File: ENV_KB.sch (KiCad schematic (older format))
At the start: 183 parts, among them J1 TYPE-C-31-M-12

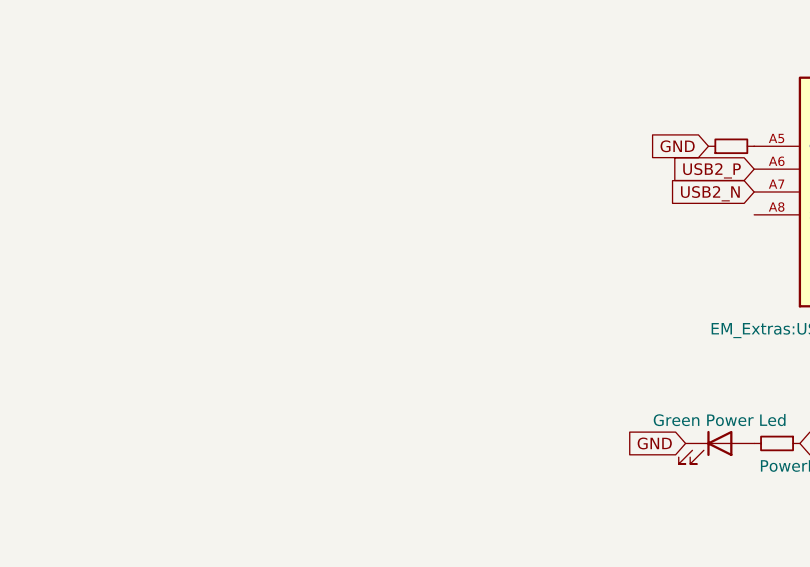
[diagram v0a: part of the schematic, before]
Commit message: Added some M2 mount holes
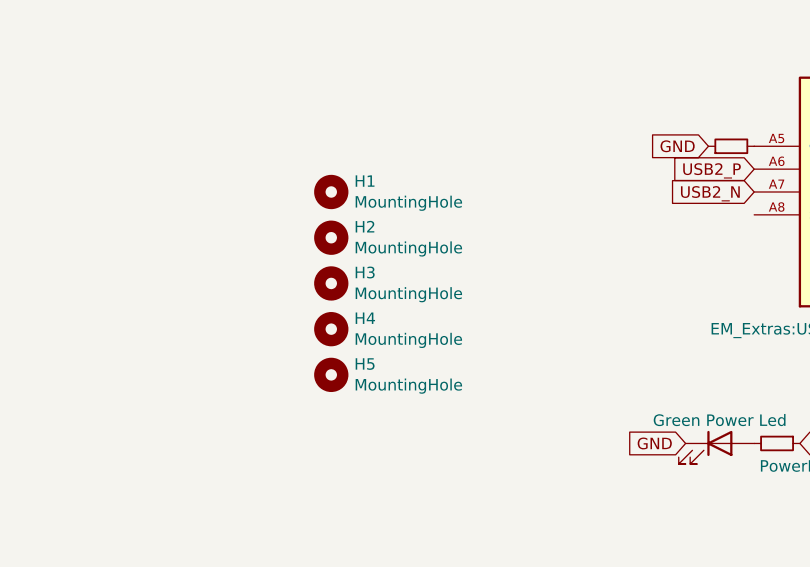
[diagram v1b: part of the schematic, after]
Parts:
- added H1, H2, H3, H4, H5: MountingHole, MountingHole:MountingHole_2.2mm_M2, symbol Mechanical:MountingHole
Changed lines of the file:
@@
 Text GLabel 13750 8250 2    50   Input ~ 0
 3.3V
+$Comp
+L Mechanical:MountingHole H4
+U 1 1 6058BC08
+P 6600 9450
+F 0 "H4" H 6700 9496 50  0000 L CNN
+F 1 "MountingHole" H 6700 9405 50  0000 L CNN
+F 2 "MountingHole:MountingHole_2.2mm_M2" H 6600 9450 50  0001 C CNN
+F 3 "~" H 6600 9450 50  0001 C CNN
+	1    6600 9450
+	1    0    0    -1
+$EndComp
+$Comp
+L Mechanical:MountingHole H3
+U 1 1 60591F15
+P 6600 9250
+F 0 "H3" H 6700 9296 50  0000 L CNN
+F 1 "MountingHole" H 6700 9205 50  0000 L CNN
+F 2 "MountingHole:MountingHole_2.2mm_M2" H 6600 9250 50  0001 C CNN
+F 3 "~" H 6600 9250 50  0001 C CNN
+	1    6600 9250
+	1    0    0    -1
+$EndComp
+$Comp
+L Mechanical:MountingHole H1
+U 1 1 605938C3
+P 6600 8850
+F 0 "H1" H 6700 8896 50  0000 L CNN
+F 1 "MountingHole" H 6700 8805 50  0000 L CNN
+F 2 "MountingHole:MountingHole_2.2mm_M2" H 6600 8850 50  0001 C CNN
+F 3 "~" H 6600 8850 50  0001 C CNN
+	1    6600 8850
+	1    0    0    -1
+$EndComp
+$Comp
+L Mechanical:MountingHole H2
+U 1 1 605BD366
+P 6600 9050
+F 0 "H2" H 6700 9096 50  0000 L CNN
+F 1 "MountingHole" H 6700 9005 50  0000 L CNN
+F 2 "MountingHole:MountingHole_2.2mm_M2" H 6600 9050 50  0001 C CNN
+F 3 "~" H 6600 9050 50  0001 C CNN
+	1    6600 9050
+	1    0    0    -1
+$EndComp
+$Comp
+L Mechanical:MountingHole H5
+U 1 1 6068A680
+P 6600 9650
+F 0 "H5" H 6700 9696 50  0000 L CNN
+F 1 "MountingHole" H 6700 9605 50  0000 L CNN
+F 2 "MountingHole:MountingHole_2.2mm_M2" H 6600 9650 50  0001 C CNN
+F 3 "~" H 6600 9650 50  0001 C CNN
+	1    6600 9650
+	1    0    0    -1
+$EndComp
 $EndSCHEMATC

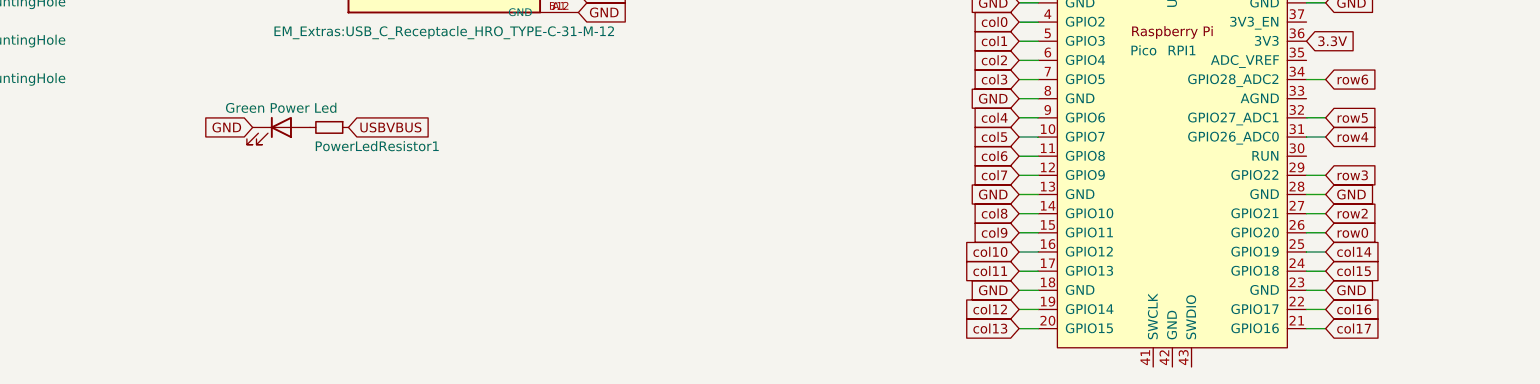
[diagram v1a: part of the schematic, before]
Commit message: Added Reset Button, Adjusted some trace routes, Updated Schematic
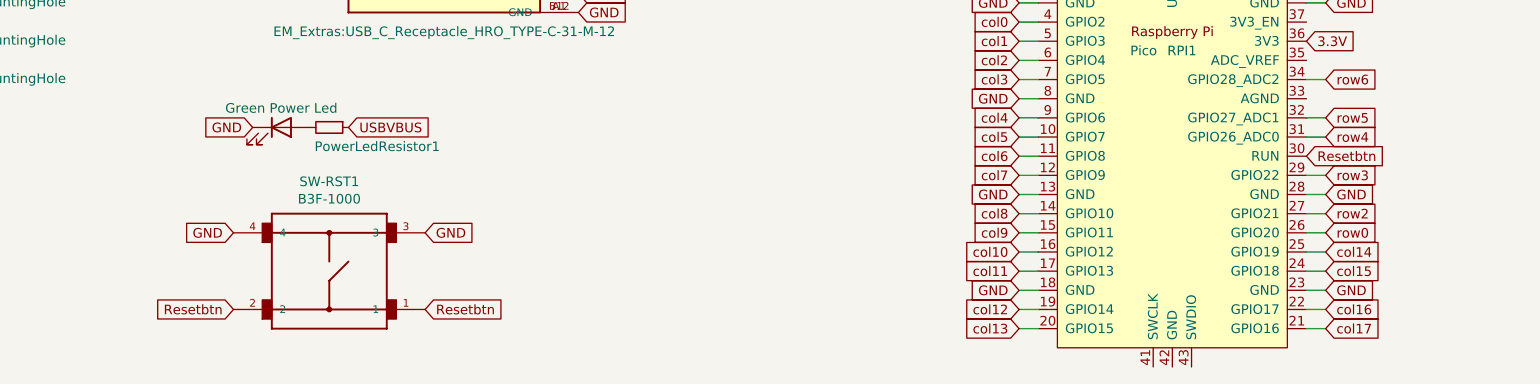
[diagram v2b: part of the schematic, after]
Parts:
- added SW-RST1: B3F-1000, EM_Extras:SW_B3F-1000, symbol B3F-1000:B3F-1000
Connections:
- net GND: now also SW-RST1.3, SW-RST1.4
- net Resetbtn: now reaches RPI1.30 (RUN)
- net Resetbtn: now also SW-RST1.1, SW-RST1.2
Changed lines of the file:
@@
 	1    0    0    -1
 $EndComp
+Text GLabel 13650 10100 2    50   Input ~ 0
+Resetbtn
+Text GLabel 9050 10500 2    50   Input ~ 0
+GND
+Text GLabel 8050 10900 0    50   Input ~ 0
+Resetbtn
+$Comp
+L B3F-1000:B3F-1000 SW-RST1
+U 1 1 605FBFA6
+P 8550 10700
+F 0 "SW-RST1" H 8550 11167 50  0000 C CNN
+F 1 "B3F-1000" H 8550 11076 50  0000 C CNN
+F 2 "EM_Extras:SW_B3F-1000" H 8550 10700 50  0001 L BNN
+F 3 "" H 8550 10700 50  0001 L BNN
+F 4 "Omron" H 8550 10700 50  0001 L BNN "MANUFACTURER"
+	1    8550 10700
+	1    0    0    -1
+$EndComp
+Text GLabel 8050 10500 0    50   Input ~ 0
+GND
+Text GLabel 9050 10900 2    50   Input ~ 0
+Resetbtn
 $EndSCHEMATC

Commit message: Initial Ansi Support
adding support to fit ansi backslash and enter key

probably needs some double checking +this would be incompatible with the current keymap unless you dont mind a non functional enter key and a ANSI backslash which does enter instead.
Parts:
- added D63: D, CFTKB Bits:D_DO-35_SOD27_P5.08mm_Horizontal, symbol Device:D_Small
- added K_63: MX-NoLED, MX_only:MXOnly-ISO-ROTATED-ReversedStabilizers-NoLED, symbol MX_Alps_Hybrid:MX-NoLED
- added K_63B1: MX-NoLED, MX_only:MXOnly-2.25U-NoLED, symbol MX_Alps_Hybrid:MX-NoLED
- added K_64B1: KEYSW, MX_only:MXOnly-2.25U-NoLED, symbol MX_Alps_Hybrid:MX-NoLED
- K_46: footprint MX_only:MXOnly-ISO-ROTATED-ReversedStabilizers-NoLED -> MX_only:MXOnly-1.5U-NoLED
- renumbered D63 to D64, D64 to D65, D65 to D66, D66 to D67, D67 to D68, D68 to D69, D69 to D70, D70 to D71, D71 to D72, D72 to D73, D73 to D74, D74 to D75, D75 to D76, D76 to D77, D77 to D78, D78 to D79, D79 to D80, D80 to D81, D81 to D82, D82 to D83, D83 to D84, D84 to D85, D85 to D86, D86 to D87, D87 to D88, H1 to H0, H2 to H1, H3 to H2, H4 to H3, H5 to H4, I2CHeader1 to I2CHeader0, J1 to J0, K_63 to K_64, K_64 to K_65, K_65 to K_66, K_66 to K_67, K_67 to K_68, K_68 to K_69, K_69 to K_70, K_70 to K_71, K_71 to K_72, K_72 to K_73, K_73 to K_74, K_74 to K_75, K_75 to K_76, K_76 to K_77, K_77 to K_78, K_78 to K_79, K_79 to K_80, K_80 to K_81, K_81 to K_82, K_82 to K_83, K_83 to K_84, K_84 to K_85, K_85 to K_86, K_86 to K_87, K_87 to K_88, PowerLED1 to PowerLED0, PowerLedResistor1 to PowerLedResistor0, RESISTOR2 to RESISTOR0, RPI1 to RPI0, SW-RST1 to SW-RST0
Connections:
- net col0: now also K_64B1.1 (COL)
- net col14: now also K_63.1 (COL), K_63B1.1 (COL)
- net row4: now also D63.1 (K)
- net at D64.2 (A), K_64.2 (ROW): now also K_64B1.2 (ROW)
- new net: D63.2 (A), K_63.2 (ROW), K_63B1.2 (ROW)

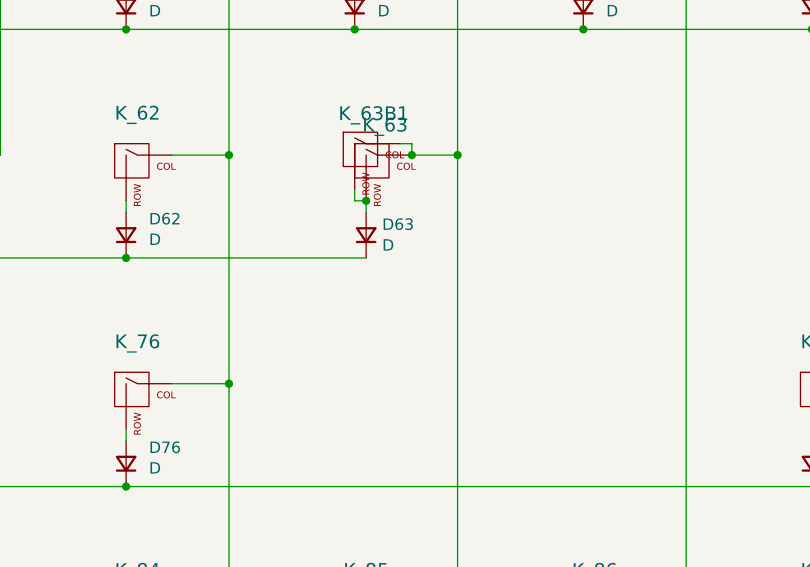
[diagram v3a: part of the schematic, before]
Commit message: ANSI updates and cleaning up
just neatened up some traces, added some markings.
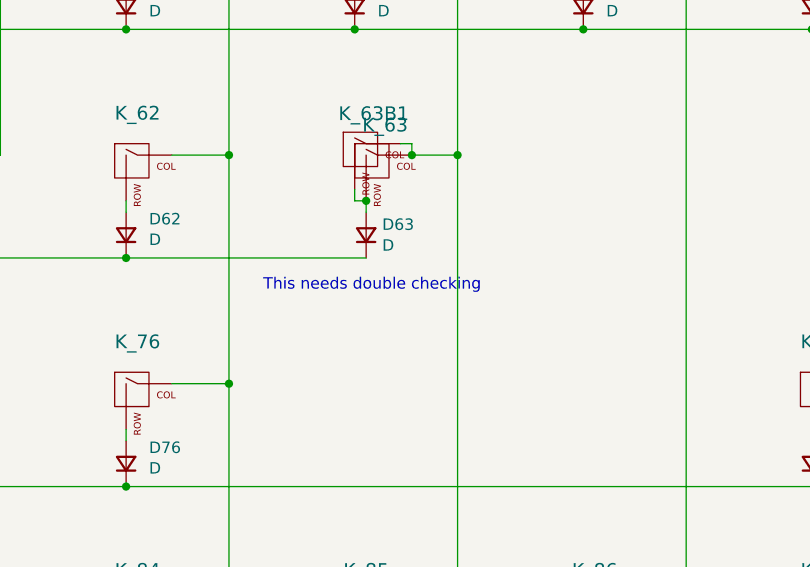
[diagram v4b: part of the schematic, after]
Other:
- note added: "This needs double checking"
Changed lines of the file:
@@
 	1550 5900 1500 5900
 Connection ~ 1550 5950
+Text Notes 14950 5550 0    50   ~ 0
+This needs double checking
 $EndSCHEMATC

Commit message: more plate design work + screwholes
I would like for this keyboard to feel like a solid unit like a individual object not an assembly of a few, something sturdy and light.
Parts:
- added H5, H6, H7, H8: MountingHole, MountingHole:MountingHole_2.2mm_M2, symbol Mechanical:MountingHole
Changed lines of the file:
@@
 Text Notes 14950 5550 0    50   ~ 0
 This needs double checking
+$Comp
+L Mechanical:MountingHole H5
+U 1 1 606F0C32
+P 6600 9850
+F 0 "H5" H 6700 9896 50  0000 L CNN
+F 1 "MountingHole" H 6700 9805 50  0000 L CNN
+F 2 "MountingHole:MountingHole_2.2mm_M2" H 6600 9850 50  0001 C CNN
+F 3 "~" H 6600 9850 50  0001 C CNN
+	1    6600 9850
+	1    0    0    -1
+$EndComp
+$Comp
+L Mechanical:MountingHole H6
+U 1 1 60748B43
+P 6600 10050
+F 0 "H6" H 6700 10096 50  0000 L CNN
+F 1 "MountingHole" H 6700 10005 50  0000 L CNN
+F 2 "MountingHole:MountingHole_2.2mm_M2" H 6600 10050 50  0001 C CNN
+F 3 "~" H 6600 10050 50  0001 C CNN
+	1    6600 10050
+	1    0    0    -1
+$EndComp
+$Comp
+L Mechanical:MountingHole H7
+U 1 1 6077360A
+P 6600 10250
+F 0 "H7" H 6700 10296 50  0000 L CNN
+F 1 "MountingHole" H 6700 10205 50  0000 L CNN
+F 2 "MountingHole:MountingHole_2.2mm_M2" H 6600 10250 50  0001 C CNN
+F 3 "~" H 6600 10250 50  0001 C CNN
+	1    6600 10250
+	1    0    0    -1
+$EndComp
+$Comp
+L Mechanical:MountingHole H8
+U 1 1 607CB78F
+P 6600 10450
+F 0 "H8" H 6700 10496 50  0000 L CNN
+F 1 "MountingHole" H 6700 10405 50  0000 L CNN
+F 2 "MountingHole:MountingHole_2.2mm_M2" H 6600 10450 50  0001 C CNN
+F 3 "~" H 6600 10450 50  0001 C CNN
+	1    6600 10450
+	1    0    0    -1
+$EndComp
 $EndSCHEMATC

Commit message: Adding more mount holes and some alignment adjustments
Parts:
- added H10, H9: MountingHole, MountingHole:MountingHole_2.2mm_M2, symbol Mechanical:MountingHole
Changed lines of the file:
@@
+	1    0    0    -1
+$EndComp
+$Comp
+L Mechanical:MountingHole H9
+U 1 1 60717F95
+P 6600 10650
+F 0 "H9" H 6700 10696 50  0000 L CNN
+F 1 "MountingHole" H 6700 10605 50  0000 L CNN
+F 2 "MountingHole:MountingHole_2.2mm_M2" H 6600 10650 50  0001 C CNN
+F 3 "~" H 6600 10650 50  0001 C CNN
+	1    6600 10650
+	1    0    0    -1
+$EndComp
+$Comp
+L Mechanical:MountingHole H10
+U 1 1 607429B3
+P 6600 10850
+F 0 "H10" H 6700 10896 50  0000 L CNN
+F 1 "MountingHole" H 6700 10805 50  0000 L CNN
+F 2 "MountingHole:MountingHole_2.2mm_M2" H 6600 10850 50  0001 C CNN
+F 3 "~" H 6600 10850 50  0001 C CNN
+	1    6600 10850
 	1    0    0    -1
 $EndComp

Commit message: Some small updates and corrections
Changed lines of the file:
@@
+	1    0    0    -1
+$EndComp
+$Comp
+L PersonalLogo:LOGO #G1
+U 1 1 607C9850
+P 5000 9700
+F 0 "#G1" H 5000 9090 60  0001 C CNN
+F 1 "LOGO" H 5000 10310 60  0001 C CNN
+F 2 "" H 5000 9700 50  0001 C CNN
+F 3 "" H 5000 9700 50  0001 C CNN
+	1    5000 9700
 	1    0    0    -1
 $EndComp

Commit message: added B§F-100o back to Symbole Lib Back pasting of my changes move of drill hole lower right side
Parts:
- removed D63: D, CFTKB Bits:D_DO-35_SOD27_P5.08mm_Horizontal, symbol Device:D_Small
- removed H10, H5, H6, H7, H8, H9: MountingHole, MountingHole:MountingHole_2.2mm_M2, symbol Mechanical:MountingHole
- removed K_63: MX-NoLED, MX_only:MXOnly-ISO-ROTATED-ReversedStabilizers-NoLED, symbol MX_Alps_Hybrid:MX-NoLED
- removed K_63B1: MX-NoLED, MX_only:MXOnly-2.25U-NoLED, symbol MX_Alps_Hybrid:MX-NoLED
- removed K_64B1: KEYSW, MX_only:MXOnly-2.25U-NoLED, symbol MX_Alps_Hybrid:MX-NoLED
- added D100, D101, D102, D103, D104, D88, D89, D90, D91, D92, D93, D94, D95, D96, D97, D98, D99: D, CFTKB Bits:D_DO-35_SOD27_P5.08mm_Horizontal, symbol Device:D_Small
- added D105: Scroll Lock, LED_THT:LED_D5.0mm, symbol Device:LED
- added D106: Cabs Lock, LED_THT:LED_D5.0mm, symbol Device:LED
- added D107: NUM Lock, LED_THT:LED_D5.0mm, symbol Device:LED
- added J2: Conn_01x03, Connector_PinSocket_2.54mm:PinSocket_1x03_P2.54mm_Vertical, symbol Connector_Generic:Conn_01x03
- added J3: Conn_01x12, Connector_PinSocket_2.54mm:PinSocket_1x12_P2.54mm_Vertical, symbol Connector_Generic:Conn_01x12
- added JP1: Adress Pin A2, Jumper:SolderJumper-2_P1.3mm_Bridged_RoundedPad1.0x1.5mm, symbol Jumper:SolderJumper_2_Bridged
- added JP2: ADress Pin A1, Jumper:SolderJumper-2_P1.3mm_Bridged_RoundedPad1.0x1.5mm, symbol Jumper:SolderJumper_2_Bridged
- added JP3: Adress Pin A0, Jumper:SolderJumper-2_P1.3mm_Bridged_RoundedPad1.0x1.5mm, symbol Jumper:SolderJumper_2_Bridged
- added K_100, K_101, K_102, K_89, K_90, K_91, K_92, K_93, K_94, K_95, K_97, K_98, K_99: KEYSW, MX_Only:MXOnly-1U-NoLED, symbol MX_Alps_Hybrid:MX-NoLED
- added K_103, K_104: KEYSW, MX_Only:MXOnly-2U-NoLED, symbol MX_Alps_Hybrid:MX-NoLED
- added K_88: Num Lock, MX_Only:MXOnly-1U-NoLED, symbol MX_Alps_Hybrid:MX-NoLED
- added K_96: KEYSW, MX_Only:MXOnly-2U-ReversedStabilizers-NoLED, symbol MX_Alps_Hybrid:MX-NoLED
- added R1, R2, R3, R4, R5: R, CFTKB Bits:R_Axial_DIN0204_L3.6mm_D1.6mm_P7.62mm_Horizontal, symbol Device:R
- added U1: MCP23017_SP, Package_DIP:DIP-28_W7.62mm, symbol Interface_Expansion:MCP23017_SP
- K_46: footprint MX_only:MXOnly-1.5U-NoLED -> MX_only:MXOnly-ISO-ROTATED-ReversedStabilizers-NoLED
- renumbered D64 to D63, D65 to D64, D66 to D65, D67 to D66, D68 to D67, D69 to D68, D70 to D69, D71 to D70, D72 to D71, D73 to D72, D74 to D73, D75 to D74, D76 to D75, D77 to D76, D78 to D77, D79 to D78, D80 to D79, D81 to D80, D82 to D81, D83 to D82, D84 to D83, D85 to D84, D86 to D85, D87 to D86, D88 to D87, H0 to H1, H1 to H2, H2 to H3, H3 to H4, H4 to H5, I2CHeader0 to I2CHeader1, J0 to J1, K_64 to K_63, K_65 to K_64, K_66 to K_65, K_67 to K_66, K_68 to K_67, K_69 to K_68, K_70 to K_69, K_71 to K_70, K_72 to K_71, K_73 to K_72, K_74 to K_73, K_75 to K_74, K_76 to K_75, K_77 to K_76, K_78 to K_77, K_79 to K_78, K_80 to K_79, K_81 to K_80, K_82 to K_81, K_83 to K_82, K_84 to K_83, K_85 to K_84, K_86 to K_85, K_87 to K_86, K_88 to K_87, PowerLED0 to PowerLED1, PowerLedResistor0 to PowerLedResistor1, RESISTOR0 to RESISTOR2, RPI0 to RPI1, SW-RST0 to SW-RST1
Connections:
- net labels added: col18, col19, col20, col21
- wire segments 396 -> 525
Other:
- note removed: "This needs double checking"
